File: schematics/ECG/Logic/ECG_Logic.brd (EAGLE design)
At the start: 29.6 x 27.7 mm, 78 parts, among them IC1 ADS1293, IC2 LIS3DH, IC3 MCP1703, IC4 CC2541, IC5 FSA4157, IC6 FSA4157, IC7 FSA4157, P1 TARGET_RA, P2 TARGET_RA, P3 TARGET_RA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

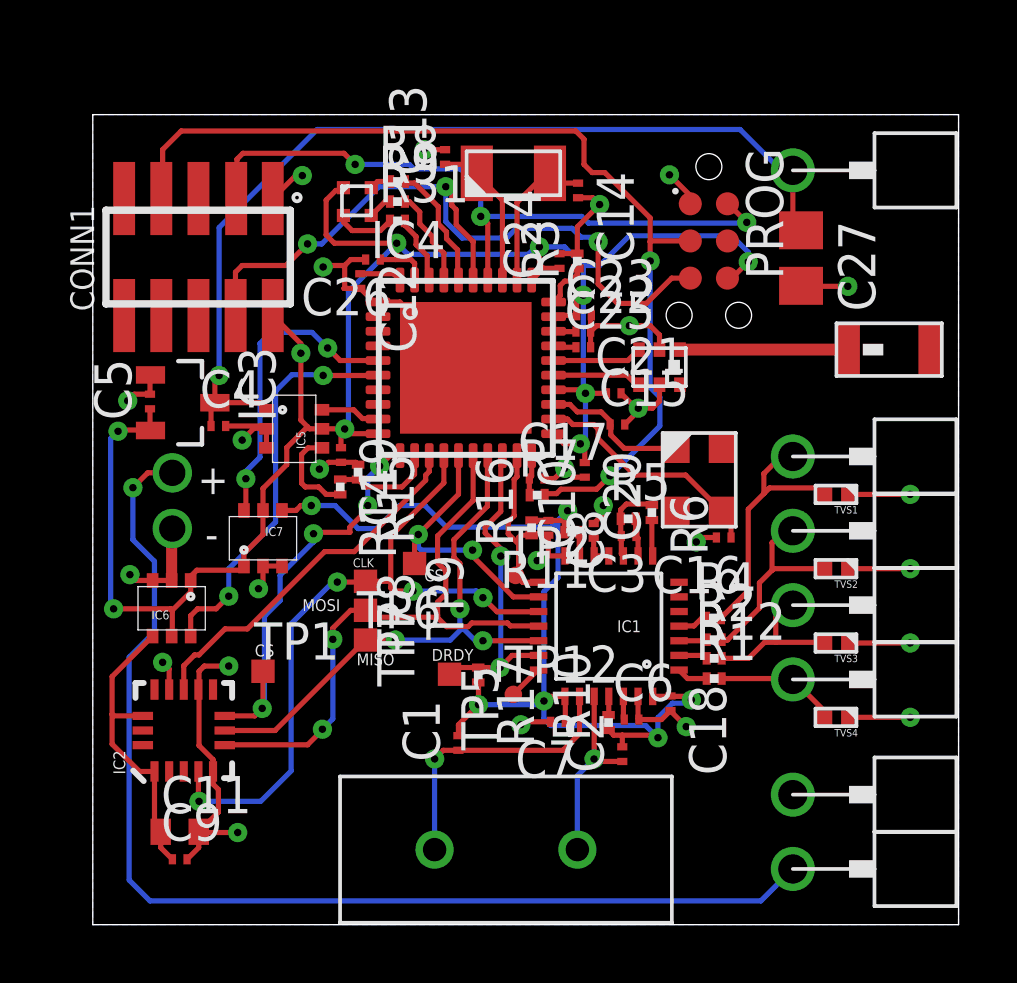
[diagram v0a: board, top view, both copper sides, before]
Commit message: RGB LED wiring was incorrect due to error in package. Using updated RGB LED package with correct wiring
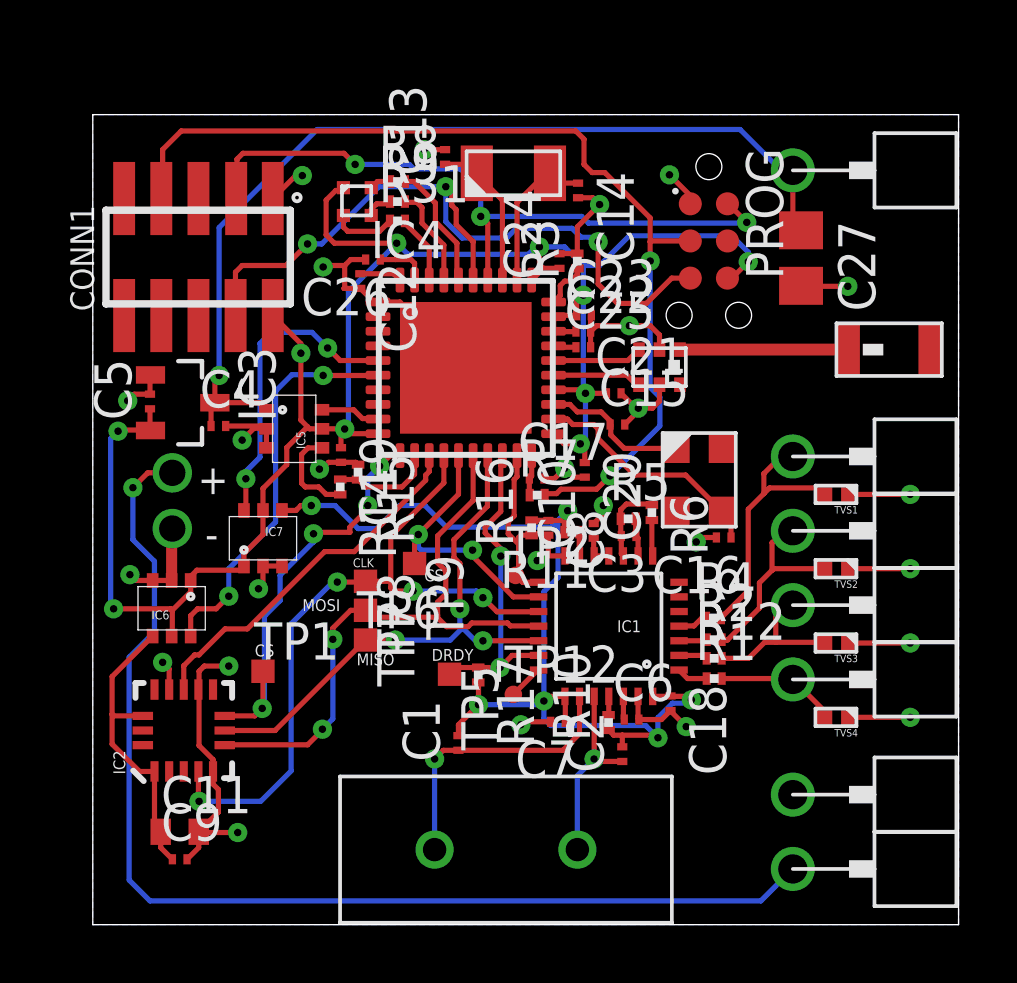
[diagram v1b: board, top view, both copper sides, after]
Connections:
- net BLUE_LED: now also IC4.37, R9.2; no longer IC4.36, R8.2
- net RED_LED: now also IC4.36, R8.2; no longer IC4.37, R9.2
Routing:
- net RED_LED: track 3.32 -> 4.30 mm
- net BLUE_LED: track 4.32 -> 3.46 mm
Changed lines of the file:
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@@
 <?xml version="1.0" encoding="utf-8"?>
 <!DOCTYPE eagle SYSTEM "eagle.dtd">
-<eagle version="6.4">
+<eagle version="6.5.0">
 <drawing>
 <settings>
@@
 <wire x1="18.0975" y1="6.0793" x2="18.0975" y2="6.477" width="0.1778" layer="1"/>
 </signal>
-<signal name="BLUE_LED">
-<contactref element="IC4" pad="36"/>
-<contactref element="R8" pad="2"/>
-<wire x1="12.4714" y1="22.0598" x2="12.4998" y2="22.0314" width="0.1778" layer="1"/>
-<wire x1="12.4714" y1="22.0598" x2="12.4714" y2="23.0632" width="0.1778" layer="1"/>
-<wire x1="10.669" y1="25.4" x2="10.669" y2="25.3482" width="0.1778" layer="1"/>
-<wire x1="11.811" y1="23.9522" x2="12.0904" y2="23.6728" width="0.1778" layer="1"/>
-<wire x1="12.0904" y1="23.6728" x2="12.0904" y2="23.4442" width="0.1778" layer="1"/>
-<wire x1="12.0904" y1="23.4442" x2="12.4714" y2="23.0632" width="0.1778" layer="1"/>
-<wire x1="10.669" y1="25.3482" x2="10.9992" y2="25.3482" width="0.1778" layer="1"/>
-<wire x1="11.811" y1="23.9522" x2="11.811" y2="24.5364" width="0.1778" layer="1"/>
-<wire x1="11.811" y1="24.5364" x2="10.9992" y2="25.3482" width="0.1778" layer="1"/>
-</signal>
 <signal name="GREEN_LED">
 <contactref element="IC4" pad="38"/>
+<wire x1="11.4808" y1="22.0504" x2="11.4998" y2="22.0314" width="0.1778" layer="1"/>
+<wire x1="11.43" y1="22.1012" x2="11.4998" y2="22.0314" width="0.1778" layer="1"/>
 <contactref element="R31" pad="2"/>
-<wire x1="11.4808" y1="22.0504" x2="11.4998" y2="22.0314" width="0.1778" layer="1"/>
-<wire x1="11.43" y1="22.86" x2="11.43" y2="22.1012" width="0.1778" layer="1"/>
-<wire x1="11.43" y1="22.1012" x2="11.4998" y2="22.0314" width="0.1778" layer="1"/>
-<wire x1="10.669" y1="24.0538" x2="10.669" y2="23.9004" width="0.1778" layer="1"/>
-<wire x1="10.669" y1="23.9004" x2="11.049" y2="23.5204" width="0.1778" layer="1"/>
-<wire x1="11.049" y1="23.5204" x2="11.049" y2="23.241" width="0.1778" layer="1"/>
-<wire x1="11.049" y1="23.241" x2="11.43" y2="22.86" width="0.1778" layer="1"/>
+<wire x1="10.669" y1="23.9766" x2="11.4998" y2="23.1458" width="0.1778" layer="1"/>
+<wire x1="11.4998" y1="22.0314" x2="11.4998" y2="23.1458" width="0.1778" layer="1"/>
+<wire x1="10.669" y1="24.0538" x2="10.669" y2="23.9766" width="0.1778" layer="1"/>
 </signal>
 <signal name="N$3">
 <contactref element="TRI_LED" pad="3"/>
 <contactref element="R9" pad="1"/>
-<wire x1="10.159" y1="24.7142" x2="9.9916" y2="24.7142" width="0.1778" layer="1"/>
-<wire x1="9.9916" y1="24.7142" x2="9.517" y2="24.2396" width="0.1778" layer="1"/>
+<wire x1="9.517" y1="24.2396" x2="9.517" y2="24.4522" width="0.1778" layer="1"/>
+<wire x1="9.517" y1="24.4522" x2="9.7028" y2="24.638" width="0.1778" layer="1"/>
+<wire x1="9.7028" y1="24.638" x2="10.0828" y2="24.638" width="0.1778" layer="1"/>
+<wire x1="10.0828" y1="24.638" x2="10.159" y2="24.7142" width="0.1778" layer="1"/>
 </signal>
 <signal name="N$9">
@@
 <contactref element="R31" pad="1"/>
 <wire x1="10.159" y1="24.0538" x2="10.159" y2="23.9512" width="0.1778" layer="1"/>
-<wire x1="8.567" y1="24.2396" x2="8.567" y2="24.0212" width="0.1778" layer="1"/>
-<wire x1="8.567" y1="24.0212" x2="8.8646" y2="23.7236" width="0.1778" layer="1"/>
-<wire x1="8.8646" y1="23.7236" x2="9.8288" y2="23.7236" width="0.1778" layer="1"/>
-<wire x1="9.8288" y1="23.7236" x2="10.159" y2="24.0538" width="0.1778" layer="1"/>
+<wire x1="8.567" y1="24.2396" x2="8.567" y2="23.8434" width="0.1778" layer="1"/>
+<wire x1="8.567" y1="23.8434" x2="8.7122" y2="23.6982" width="0.1778" layer="1"/>
+<wire x1="8.7122" y1="23.6982" x2="9.8034" y2="23.6982" width="0.1778" layer="1"/>
+<wire x1="9.8034" y1="23.6982" x2="10.159" y2="24.0538" width="0.1778" layer="1"/>
 </signal>
 <signal name="N$20">
@@
 </signal>
 <signal name="RED_LED">
-<contactref element="R9" pad="2"/>
-<contactref element="IC4" pad="37"/>
-<wire x1="11.9998" y1="22.0314" x2="11.9998" y2="22.9506" width="0.1778" layer="1"/>
-<wire x1="10.669" y1="24.7142" x2="10.8204" y2="24.7142" width="0.1778" layer="1"/>
-<wire x1="10.8204" y1="24.7142" x2="11.176" y2="24.3586" width="0.1778" layer="1"/>
-<wire x1="11.176" y1="24.3586" x2="11.176" y2="23.9522" width="0.1778" layer="1"/>
-<wire x1="11.176" y1="23.9522" x2="11.6078" y2="23.5204" width="0.1778" layer="1"/>
-<wire x1="11.6078" y1="23.5204" x2="11.6078" y2="23.3426" width="0.1778" layer="1"/>
-<wire x1="11.6078" y1="23.3426" x2="11.9998" y2="22.9506" width="0.1778" layer="1"/>
+<contactref element="IC4" pad="36"/>
+<contactref element="R8" pad="2"/>
+<wire x1="11.7094" y1="24.0284" x2="11.7094" y2="24.6634" width="0.1778" layer="1"/>
+<wire x1="11.7094" y1="24.6634" x2="10.9728" y2="25.4" width="0.1778" layer="1"/>
+<wire x1="10.669" y1="25.4" x2="10.9728" y2="25.4" width="0.1778" layer="1"/>
+<wire x1="11.7094" y1="24.0284" x2="12.446" y2="23.2918" width="0.1778" layer="1"/>
+<wire x1="12.446" y1="23.2918" x2="12.446" y2="22.0852" width="0.1778" layer="1"/>
+<wire x1="12.446" y1="22.0852" x2="12.4998" y2="22.0314" width="0.1778" layer="1"/>
 </signal>
 <signal name="N$6">
@@
 <wire x1="23.9268" y1="24.0132" x2="24.2062" y2="23.7338" width="0.1778" layer="1"/>
 </signal>
+<signal name="BLUE_LED">
+<contactref element="IC4" pad="37"/>
+<contactref element="R9" pad="2"/>
+<wire x1="11.2522" y1="24.511" x2="11.0744" y2="24.6888" width="0.1778" layer="1"/>
+<wire x1="11.0744" y1="24.6888" x2="10.6944" y2="24.6888" width="0.1778" layer="1"/>
+<wire x1="10.6944" y1="24.6888" x2="10.669" y2="24.7142" width="0.1778" layer="1"/>
+<wire x1="11.2522" y1="24.511" x2="11.2522" y2="23.9776" width="0.1778" layer="1"/>
+<wire x1="11.2522" y1="23.9776" x2="11.9998" y2="23.23" width="0.1778" layer="1"/>
+<wire x1="11.9998" y1="22.0314" x2="11.9998" y2="23.23" width="0.1778" layer="1"/>
+</signal>
 </signals>

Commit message: using updated millmax target package with correctly centered origin
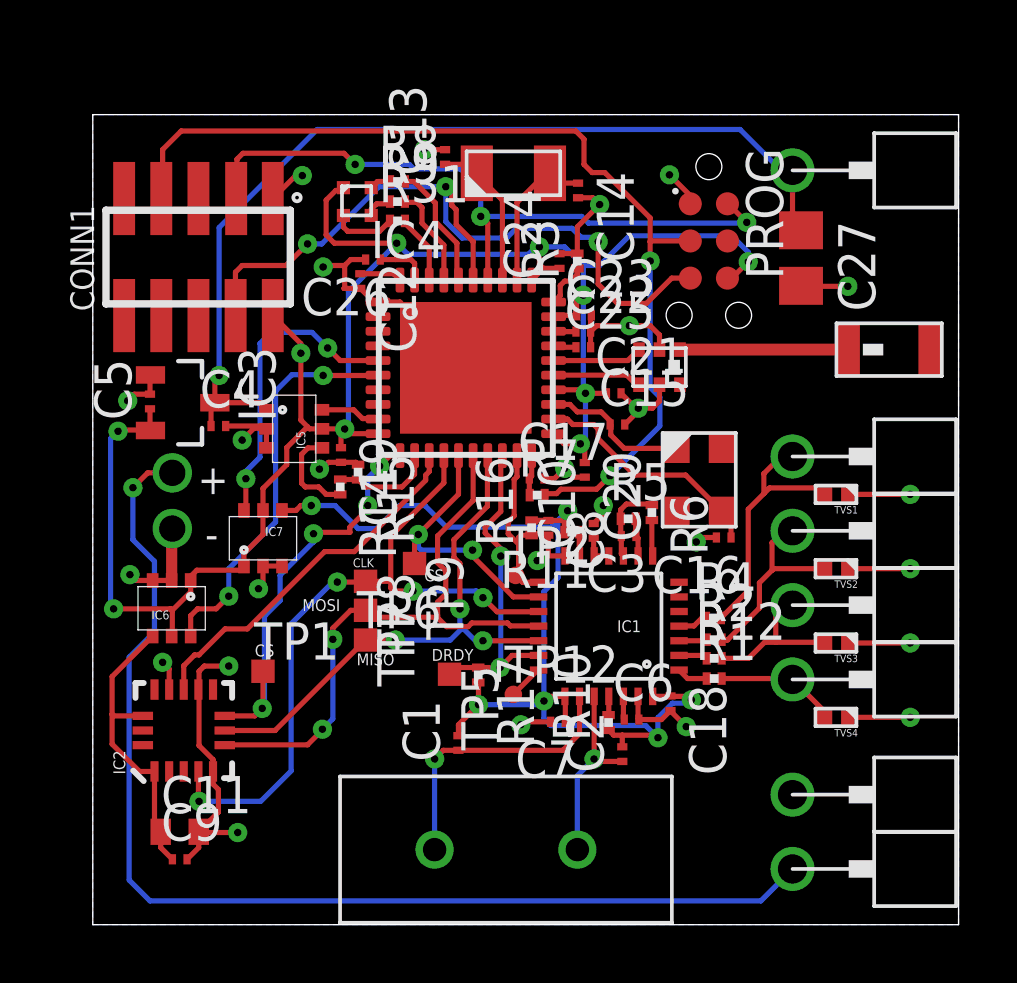
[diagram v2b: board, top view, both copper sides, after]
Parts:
- moved P1 2.82 mm to (26.7, 13.5)
- moved P2 2.82 mm to (26.7, 10.9)
- moved P3 2.82 mm to (26.7, 8.38)
- moved P4 2.82 mm to (26.7, 16.0)
- moved P5 2.82 mm to (26.7, 4.45)
- moved P6 2.82 mm to (26.7, 1.91)
- moved P7 2.82 mm to (26.7, 25.8)
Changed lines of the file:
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@@
 <attribute name="TP_SIGNAL_NAME" value="" x="14.4526" y="11.938" size="1.778" layer="27" display="off"/>
 </element>
-<element name="P1" library="pins" package="TARGET_RA" value="TARGET_RA" x="23.9268" y="13.462"/>
-<element name="P2" library="pins" package="TARGET_RA" value="TARGET_RA" x="23.9268" y="10.922"/>
-<element name="P3" library="pins" package="TARGET_RA" value="TARGET_RA" x="23.9268" y="8.382"/>
-<element name="P4" library="pins" package="TARGET_RA" value="TARGET_RA" x="23.9268" y="16.002"/>
-<element name="P5" library="pins" package="TARGET_RA" value="TARGET_RA" x="23.9268" y="4.445"/>
-<element name="P6" library="pins" package="TARGET_RA" value="TARGET_RA" x="23.9268" y="1.905"/>
-<element name="P7" library="pins" package="TARGET_RA" value="TARGET_RA" x="23.9268" y="25.781"/>
+<element name="P1" library="pins" package="TARGET_RA" value="TARGET_RA" x="26.7462" y="13.462"/>
+<element name="P2" library="pins" package="TARGET_RA" value="TARGET_RA" x="26.7462" y="10.922"/>
+<element name="P3" library="pins" package="TARGET_RA" value="TARGET_RA" x="26.7462" y="8.382"/>
+<element name="P4" library="pins" package="TARGET_RA" value="TARGET_RA" x="26.7462" y="16.002"/>
+<element name="P5" library="pins" package="TARGET_RA" value="TARGET_RA" x="26.7462" y="4.445"/>
+<element name="P6" library="pins" package="TARGET_RA" value="TARGET_RA" x="26.7462" y="1.905"/>
+<element name="P7" library="pins" package="TARGET_RA" value="TARGET_RA" x="26.7462" y="25.781"/>
 <element name="X3" library="ecs" package="ECS-40-20-4VX" value="ECS-40-20-4VX" x="14.1224" y="2.5654"/>
 <element name="C1" library="rcl" package="C0201" value="20pF" x="12.4968" y="6.2103" rot="R90"/>
@@
 <contactref element="P3" pad="1"/>
 <wire x1="21.494" y1="8.4126" x2="23.8962" y2="8.4126" width="0.1778" layer="1"/>
-<wire x1="23.8962" y1="8.4126" x2="23.9268" y2="8.382" width="0.1778" layer="1"/>
 <wire x1="25.0008" y1="7.0866" x2="25.0008" y2="7.308" width="0.1778" layer="1"/>
-<wire x1="25.0008" y1="7.308" x2="23.9268" y2="8.382" width="0.1778" layer="1"/>
+<wire x1="23.8962" y1="8.4126" x2="23.8962" y2="8.402" width="0.1778" layer="1"/>
+<wire x1="23.8962" y1="8.402" x2="23.9162" y2="8.382" width="0.1778" layer="1"/>
+<wire x1="25.0008" y1="7.308" x2="24.9902" y2="7.308" width="0.1778" layer="1"/>
+<wire x1="24.9902" y1="7.308" x2="23.9162" y2="8.382" width="0.1778" layer="1"/>
 </signal>
 <signal name="LL">
@@
 <wire x1="22.7838" y1="10.8204" x2="22.7838" y2="11.684" width="0.1778" layer="1"/>
 <wire x1="22.7838" y1="11.684" x2="23.2156" y2="12.1158" width="0.1778" layer="1"/>
-<wire x1="23.9268" y1="13.462" x2="23.622" y2="13.462" width="0.1778" layer="1"/>
+<wire x1="23.9162" y1="13.462" x2="23.622" y2="13.462" width="0.1778" layer="1"/>
 <wire x1="23.622" y1="13.462" x2="23.2156" y2="13.0556" width="0.1778" layer="1"/>
 <wire x1="23.2156" y1="13.0556" x2="23.2156" y2="12.1158" width="0.1778" layer="1"/>
@@
 <wire x1="22.4028" y1="14.1986" x2="22.9362" y2="14.732" width="0.1778" layer="1"/>
 <wire x1="24.9754" y1="14.732" x2="25.0008" y2="14.7066" width="0.1778" layer="1"/>
-<wire x1="23.9268" y1="16.002" x2="23.5204" y2="16.002" width="0.1778" layer="1"/>
+<wire x1="23.9162" y1="16.002" x2="23.5204" y2="16.002" width="0.1778" layer="1"/>
 <wire x1="23.5204" y1="16.002" x2="22.9362" y2="15.4178" width="0.1778" layer="1"/>
 <wire x1="22.9362" y1="15.4178" x2="22.9362" y2="14.732" width="0.1778" layer="1"/>
@@
 <wire x1="22.4118" y1="9.1022" x2="22.9616" y2="9.652" width="0.1778" layer="1"/>
 <wire x1="22.9616" y1="9.652" x2="23.3426" y2="9.652" width="0.1778" layer="1"/>
-<wire x1="23.9268" y1="10.922" x2="23.5458" y2="10.922" width="0.1778" layer="1"/>
+<wire x1="23.9162" y1="10.922" x2="23.5458" y2="10.922" width="0.1778" layer="1"/>
 <wire x1="23.5458" y1="10.922" x2="23.3426" y2="10.7188" width="0.1778" layer="1"/>
 <wire x1="23.3426" y1="10.7188" x2="23.3426" y2="9.652" width="0.1778" layer="1"/>
@@
 <wire x1="1.2446" y1="1.524" x2="1.9558" y2="0.8128" width="0.1778" layer="16"/>
 <wire x1="1.9558" y1="0.8128" x2="22.8346" y2="0.8128" width="0.1778" layer="16"/>
-<wire x1="22.8346" y1="0.8128" x2="23.9268" y2="1.905" width="0.1778" layer="16"/>
 <wire x1="1.8796" y1="15.4432" x2="2.7178" y2="15.4432" width="0.1778" layer="1"/>
+<wire x1="23.9162" y1="1.905" x2="23.9162" y2="1.8944" width="0.1778" layer="16"/>
+<wire x1="23.9162" y1="1.8944" x2="22.8346" y2="0.8128" width="0.1778" layer="16"/>
 </signal>
 <signal name="BATT_CHECK_SW">
@@
 <wire x1="7.6708" y1="27.178" x2="22.1234" y2="27.178" width="0.1778" layer="16"/>
 <wire x1="23.5204" y1="25.781" x2="22.1234" y2="27.178" width="0.1778" layer="16"/>
-<wire x1="23.9268" y1="25.781" x2="23.5204" y2="25.781" width="0.1778" layer="16"/>
+<wire x1="23.9162" y1="25.781" x2="23.5204" y2="25.781" width="0.1778" layer="16"/>
 <wire x1="4.318" y1="18.7706" x2="4.318" y2="23.8252" width="0.1778" layer="16"/>
 <wire x1="4.318" y1="23.8252" x2="7.6708" y2="27.178" width="0.1778" layer="16"/>
@@
 <wire x1="5.6912" y1="17.8396" x2="5.9338" y2="17.597" width="0.1778" layer="1"/>
 <contactref element="C27" pad="1"/>
-<wire x1="23.9268" y1="25.781" x2="23.9268" y2="24.0132" width="0.1778" layer="1"/>
 <wire x1="23.9268" y1="24.0132" x2="24.2062" y2="23.7338" width="0.1778" layer="1"/>
+<wire x1="23.9162" y1="25.781" x2="23.9162" y2="24.0238" width="0.1778" layer="1"/>
+<wire x1="23.9162" y1="24.0238" x2="24.2062" y2="23.7338" width="0.1778" layer="1"/>
 </signal>
 <signal name="BLUE_LED">
